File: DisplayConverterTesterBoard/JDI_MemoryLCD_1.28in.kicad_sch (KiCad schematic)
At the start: 6 parts, among them J6 Conn_01x03, J7 FPC 10PIN P0.5mm

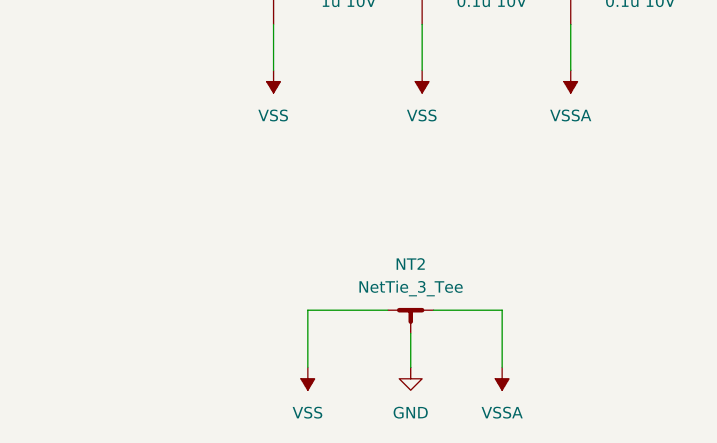
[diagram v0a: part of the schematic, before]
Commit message: fix ERCs
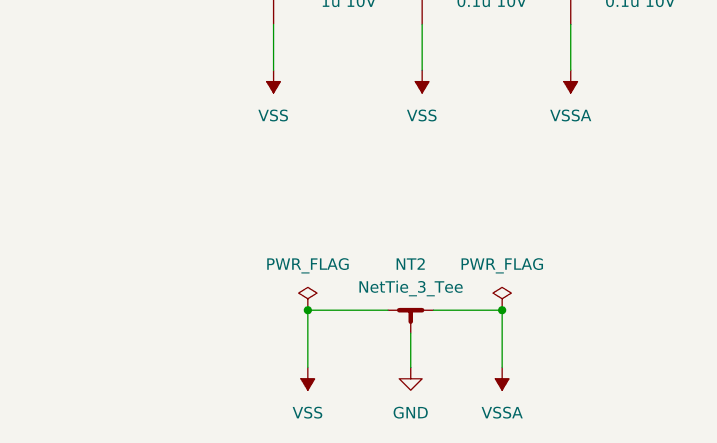
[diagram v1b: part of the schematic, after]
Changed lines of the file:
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@@
 (kicad_sch (version 20230121) (generator eeschema)
   (paper "A4")
+  (junction (at 151.13 170.18) (diameter 0) (color 0 0 0 0)
+  )
+  (junction (at 129.54 170.18) (diameter 0) (color 0 0 0 0)
+  )
   (wire (pts (xy 72.39 83.82) (xy 81.28 83.82))
     (stroke (width 0) (type default))
@@
         )
       )
+    )
+  )
+  (symbol (lib_id "power:PWR_FLAG") (at 129.54 170.18 0) (unit 1)
+    (in_bom yes) (on_board yes) (dnp no) (fields_autoplaced)
+    (property "Reference" "#FLG0401" (at 129.54 168.275 0)
+      (effects (font (size 1.27 1.27)) hide)
+    )
+    (property "Value" "PWR_FLAG" (at 129.54 165.1 0)
+      (effects (font (size 1.27 1.27)))
+    )
+    (property "Footprint" "" (at 129.54 170.18 0)
+      (effects (font (size 1.27 1.27)) hide)
+    )
+    (property "Datasheet" "~" (at 129.54 170.18 0)
+      (effects (font (size 1.27 1.27)) hide)
+    )
+    (pin "1")
+    (instances
+      (project "DisplayConverterTesterBoard"
+        (path "/58d9d6aa-d5e3-4b7b-b546-d57c329de758/0cb4f2ca-84b3-4b7f-ac05-316b1c40137b"
+          (reference "#FLG0401") (unit 1)
+        )
+      )
+    )
+  )
+  (symbol (lib_id "power:PWR_FLAG") (at 151.13 170.18 0) (unit 1)
+    (in_bom yes) (on_board yes) (dnp no) (fields_autoplaced)
+    (property "Reference" "#FLG0402" (at 151.13 168.275 0)
+      (effects (font (size 1.27 1.27)) hide)
+    )
+    (property "Value" "PWR_FLAG" (at 151.13 165.1 0)
+      (effects (font (size 1.27 1.27)))
+    )
+    (property "Footprint" "" (at 151.13 170.18 0)
+      (effects (font (size 1.27 1.27)) hide)
+    )
+    (property "Datasheet" "~" (at 151.13 170.18 0)
+      (effects (font (size 1.27 1.27)) hide)
+    )
+    (pin "1")
+    (instances
+      (project "DisplayConverterTesterBoard"
+        (path "/58d9d6aa-d5e3-4b7b-b546-d57c329de758/0cb4f2ca-84b3-4b7f-ac05-316b1c40137b"
+          (reference "#FLG0402") (unit 1)
+        )
+      )
